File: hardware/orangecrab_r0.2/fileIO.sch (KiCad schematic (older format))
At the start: 26 parts, among them J1 Conn_01x12_Male, J2 Conn_01x16_Male, J3 USB_B_Micro, SW1 SW_Push, U9 CD74HC4067M

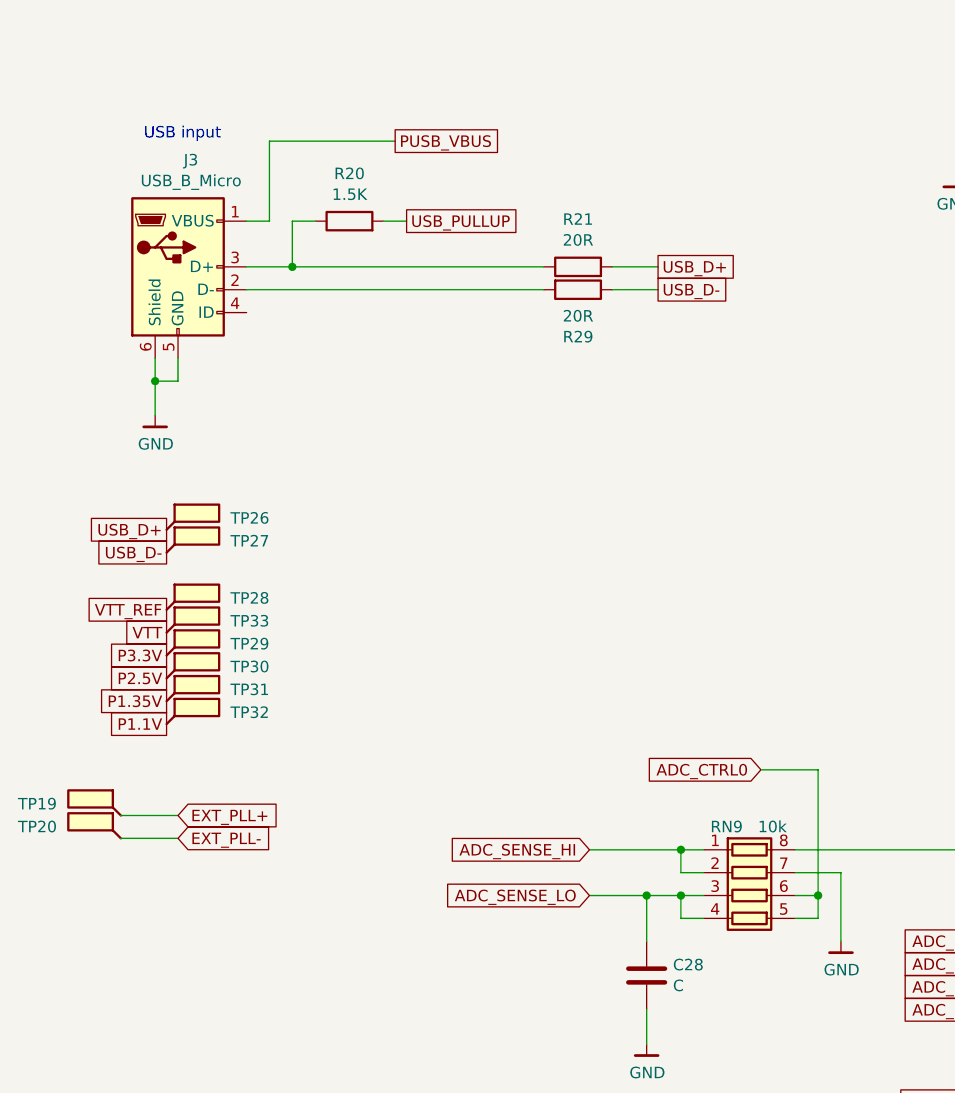
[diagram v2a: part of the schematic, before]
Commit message: hw: Update board with 3d models Finish pin-swaps and routing of open changes General cleanups
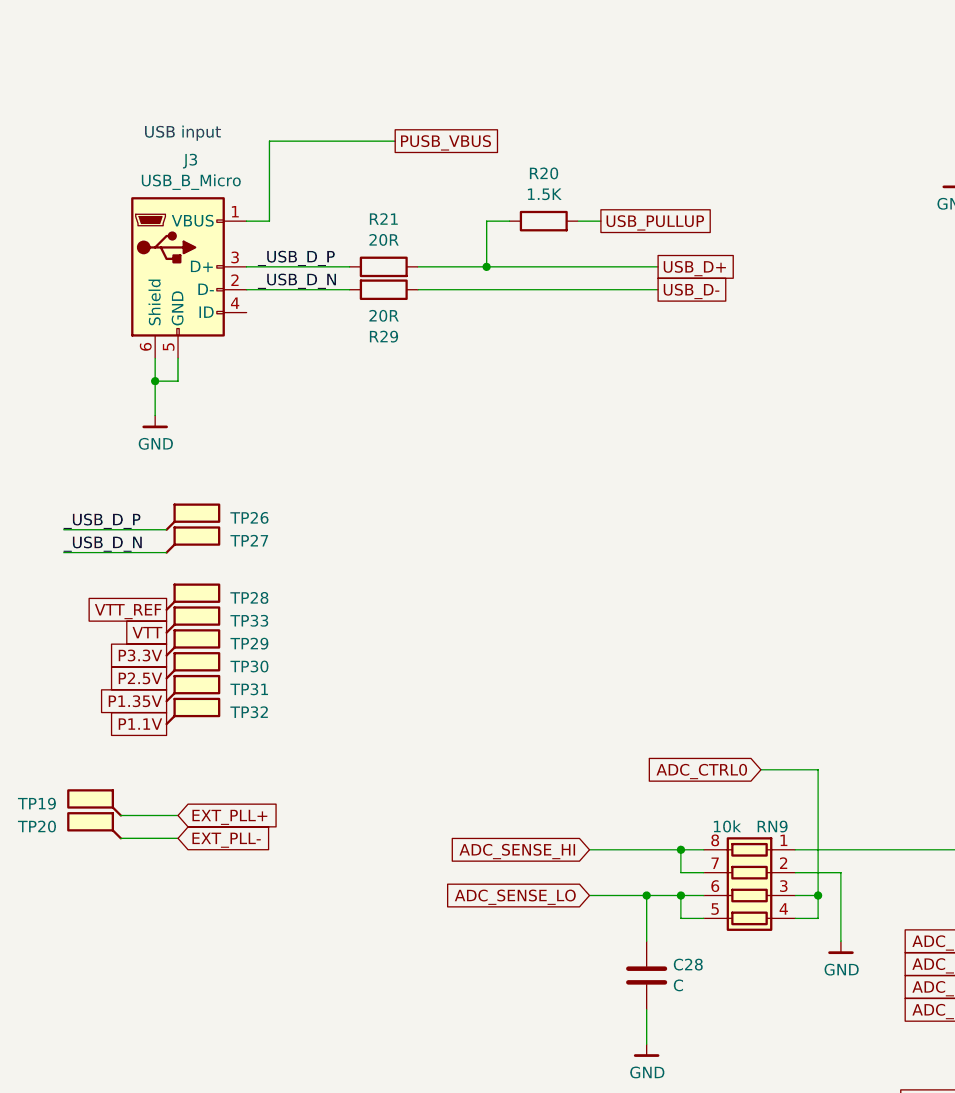
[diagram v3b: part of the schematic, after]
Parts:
- R21, R29: PN RC0201FR-071K5L -> (none)
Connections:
- net ADC_CTRL0: now also RN9.3 (R3.1), RN9.4 (R4.1); no longer RN9.5 (R4.2), RN9.6 (R3.2)
- net ADC_SENSE_HI: now also RN9.7 (R2.2), RN9.8 (R1.2); no longer RN9.1 (R1.1), RN9.2 (R2.1)
- net ADC_SENSE_LO: now also RN9.5 (R4.2), RN9.6 (R3.2); no longer RN9.3 (R3.1), RN9.4 (R4.1)
- net GND: now also RN9.2 (R2.1); no longer RN9.7 (R2.2)
- net USB_D+: now also R20.1; no longer TP26.1
- net USB_D-: no longer TP27.1
- net _USB_D_N: now reaches J3.2 (D-), R29.2
- net _USB_D_N: now also TP27.1
- net _USB_D_P: now reaches J3.3 (D+), R21.1
- net _USB_D_P: now also TP26.1; no longer R20.1
- net at U9.1 (COM): now also RN9.1 (R1.1); no longer RN9.8 (R1.2)
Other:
- moved on the sheet: R20, R21, R29
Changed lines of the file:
@@
 USB_D-
-Wire Wire Line
-	2100 1750 2300 1750
-Wire Wire Line
-	3900 1850 3700 1850
 Wire Wire Line
 	1800 2150 1800 2250
@@
 	1    0    0    -1
 $EndComp
-Text GLabel 2800 1550 2    50   UnSpc ~ 0
+Text GLabel 3650 1550 2    50   UnSpc ~ 0
 USB_PULLUP
 $Comp
 L Device:R R20
 U 1 1 5D4D2223
-P 2550 1550
-F 0 "R20" V 2757 1550 50  0000 C CNN
-F 1 "1.5K" V 2666 1550 50  0000 C CNN
-F 2 "Resistor_SMD:R_0201_0603Metric" V 2480 1550 50  0001 C CNN
-F 3 "~" H 2550 1550 50  0001 C CNN
-F 4 "‎Yageo‎" H 2550 1550 50  0001 C CNN "Mfg"
-F 5 "RC0201FR-071K5L" H 2550 1550 50  0001 C CNN "PN"
-	1    2550 1550
+P 3400 1550
+F 0 "R20" V 3607 1550 50  0000 C CNN
+F 1 "1.5K" V 3516 1550 50  0000 C CNN
+F 2 "Resistor_SMD:R_0201_0603Metric" V 3330 1550 50  0001 C CNN
+F 3 "~" H 3400 1550 50  0001 C CNN
+F 4 "‎Yageo‎" H 3400 1550 50  0001 C CNN "Mfg"
+F 5 "RC0201FR-071K5L" H 3400 1550 50  0001 C CNN "PN"
+	1    3400 1550
 	0    -1   -1   0
 $EndComp
 Wire Wire Line
-	2400 1550 2300 1550
-Wire Wire Line
-	2300 1550 2300 1750
-Connection ~ 2300 1750
-Wire Wire Line
-	2300 1750 3400 1750
-Wire Wire Line
-	2700 1550 2800 1550
+	3250 1550 3150 1550
+Wire Wire Line
+	3150 1550 3150 1750
+Wire Wire Line
+	3550 1550 3650 1550
 Wire Wire Line
 	2100 1550 2200 1550
@@
 	1    0    0    -1
 $EndComp
-Text GLabel 1750 2900 0    50   UnSpc ~ 0
-USB_D+
-Text GLabel 1750 3000 0    50   UnSpc ~ 0
-USB_D-
 $Comp
 L Connector:TestPoint_Flag TP31
@@
 L Device:R R21
 U 1 1 5DEC8B60
-P 3550 1750
-F 0 "R21" V 3757 1750 50  0000 C CNN
-F 1 "20R" V 3666 1750 50  0000 C CNN
-F 2 "Resistor_SMD:R_0201_0603Metric" V 3480 1750 50  0001 C CNN
-F 3 "~" H 3550 1750 50  0001 C CNN
-F 4 "‎Yageo‎" H 3550 1750 50  0001 C CNN "Mfg"
-F 5 "RC0201FR-071K5L" H 3550 1750 50  0001 C CNN "PN"
-	1    3550 1750
+P 2700 1750
+F 0 "R21" V 2907 1750 50  0000 C CNN
+F 1 "20R" V 2816 1750 50  0000 C CNN
+F 2 "Resistor_SMD:R_0201_0603Metric" V 2630 1750 50  0001 C CNN
+F 3 "~" H 2700 1750 50  0001 C CNN
+F 4 "‎Yageo‎" H 2700 1750 50  0001 C CNN "Mfg"
+	1    2700 1750
 	0    -1   -1   0
 $EndComp
-Wire Wire Line
-	3700 1750 3900 1750
 $Comp
 L Device:R R29
 U 1 1 5DECD575
-P 3550 1850
-F 0 "R29" V 3757 1850 50  0000 C CNN
-F 1 "20R" V 3666 1850 50  0000 C CNN
-F 2 "Resistor_SMD:R_0201_0603Metric" V 3480 1850 50  0001 C CNN
-F 3 "~" H 3550 1850 50  0001 C CNN
-F 4 "‎Yageo‎" H 3550 1850 50  0001 C CNN "Mfg"
-F 5 "RC0201FR-071K5L" H 3550 1850 50  0001 C CNN "PN"
-	1    3550 1850
+P 2700 1850
+F 0 "R29" V 2907 1850 50  0000 C CNN
+F 1 "20R" V 2816 1850 50  0000 C CNN
+F 2 "Resistor_SMD:R_0201_0603Metric" V 2630 1850 50  0001 C CNN
+F 3 "~" H 2700 1850 50  0001 C CNN
+F 4 "‎Yageo‎" H 2700 1850 50  0001 C CNN "Mfg"
+	1    2700 1850
 	0    1    1    0
 $EndComp
-Wire Wire Line
-	3400 1850 2100 1850
 $Comp
 L 74xx:CD74HC4067M U9
@@
 F 4 "Stackpole Electronics Inc" H 4300 4500 50  0001 C CNN "Mfg"
 	1    4300 4500
-	0    1    1    0
+	0    -1   1    0
 $EndComp
 Wire Wire Line
@@
 Wire Wire Line
 	6550 5300 6550 5200
+Connection ~ 3150 1750
+Wire Wire Line
+	2100 1750 2550 1750
+Wire Wire Line
+	2850 1750 3150 1750
+Wire Wire Line
+	2550 1850 2100 1850
+Wire Wire Line
+	2850 1850 3900 1850
+Wire Wire Line
+	3150 1750 3900 1750
+Text Label 2150 1750 0    50   ~ 0
+_USB_D_P
+Text Label 2150 1850 0    50   ~ 0
+_USB_D_N
+Text Label 1300 2900 0    50   ~ 0
+_USB_D_P
+Text Label 1300 3000 0    50   ~ 0
+_USB_D_N
+Wire Wire Line
+	1750 2900 1300 2900
+Wire Wire Line
+	1300 3000 1750 3000
 $EndSCHEMATC

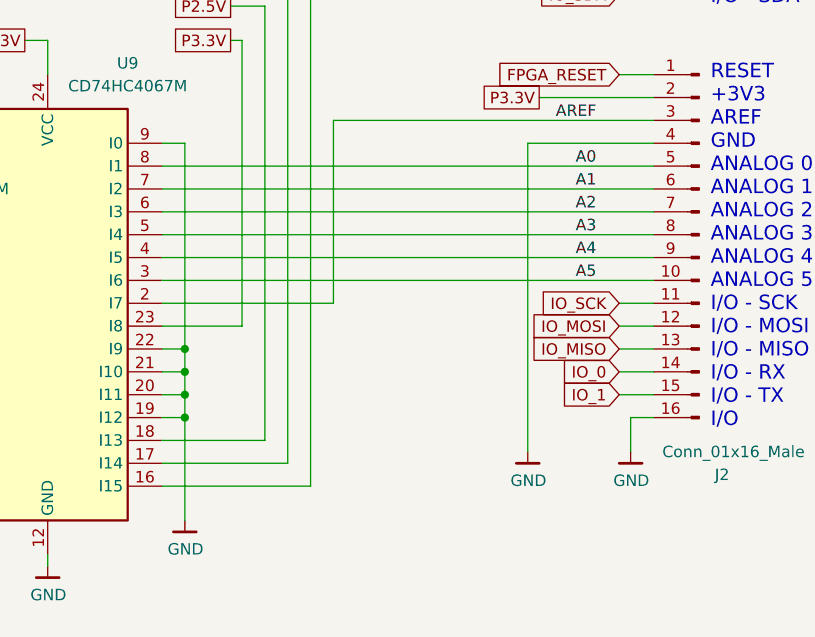
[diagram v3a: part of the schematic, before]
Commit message: hw: Route last FPGA I/O to A[0-5]
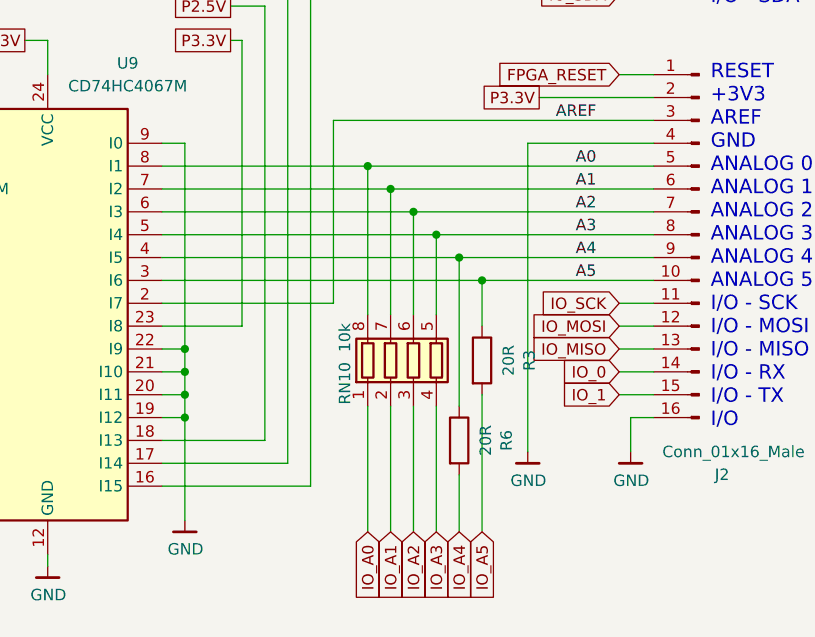
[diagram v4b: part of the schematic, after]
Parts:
- added R3, R6: 20R, Resistor_SMD:R_0201_0603Metric, symbol Device:R
- added RN10: 10k, Resistor_SMD:R_Array_Convex_4x0402, symbol Device:R_Pack04
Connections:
- net A0: now also RN10.8 (R1.2)
- net A1: now also RN10.7 (R2.2)
- net A2: now also RN10.6 (R3.2)
- net A3: now also RN10.5 (R4.2)
- net A4: now also R6.1
- net A5: now also R3.1
- new net IO_A0: RN10.1 (R1.1)
- new net IO_A1: RN10.2 (R2.1)
- new net IO_A2: RN10.3 (R3.1)
- new net IO_A3: RN10.4 (R4.1)
- new net IO_A4: R6.2
- new net IO_A5: R3.2
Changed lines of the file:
@@
 	6550 4100 6450 4100
 Wire Wire Line
-	6450 4200 8600 4200
-Wire Wire Line
-	6450 4300 8600 4300
-Wire Wire Line
-	6450 4400 8600 4400
-Wire Wire Line
-	6450 4500 8600 4500
-Wire Wire Line
-	6450 4600 8600 4600
-Wire Wire Line
-	6450 4700 8600 4700
+	6450 4200 7350 4200
+Wire Wire Line
+	6450 4300 7450 4300
+Wire Wire Line
+	6450 4400 7550 4400
+Wire Wire Line
+	6450 4500 7650 4500
+Wire Wire Line
+	6450 4700 7850 4700
 $Comp
 L gkl_power:GND #PWR0131
@@
 Wire Wire Line
 	1300 3000 1750 3000
+Text GLabel 7350 5800 3    50   Input ~ 0
+IO_A0
+Text GLabel 7450 5800 3    50   Input ~ 0
+IO_A1
+Text GLabel 7550 5800 3    50   Input ~ 0
+IO_A2
+Text GLabel 7650 5800 3    50   Input ~ 0
+IO_A3
+Text GLabel 7750 5800 3    50   Input ~ 0
+IO_A4
+Text GLabel 7850 5800 3    50   Input ~ 0
+IO_A5
+Wire Wire Line
+	7350 5800 7350 5250
+Connection ~ 7350 4200
+Wire Wire Line
+	7350 4200 8600 4200
+Wire Wire Line
+	7450 5800 7450 5250
+Connection ~ 7450 4300
+Wire Wire Line
+	7450 4300 8600 4300
+Wire Wire Line
+	7550 5800 7550 5250
+Connection ~ 7550 4400
+Wire Wire Line
+	7550 4400 8600 4400
+Wire Wire Line
+	7650 5800 7650 5250
+Connection ~ 7650 4500
+Wire Wire Line
+	7650 4500 8600 4500
+Wire Wire Line
+	7750 5800 7750 5550
+Wire Wire Line
+	7850 5800 7850 5200
+Connection ~ 7850 4700
+Wire Wire Line
+	7850 4700 8600 4700
+Wire Wire Line
+	7350 4850 7350 4200
+Wire Wire Line
+	7450 4850 7450 4300
+Wire Wire Line
+	7550 4850 7550 4400
+Wire Wire Line
+	7650 4850 7650 4500
+$Comp
+L Device:R R6
+U 1 1 5E8EF689
+P 7750 5400
+F 0 "R6" V 7957 5400 50  0000 C CNN
+F 1 "20R" V 7866 5400 50  0000 C CNN
+F 2 "Resistor_SMD:R_0201_0603Metric" V 7680 5400 50  0001 C CNN
+F 3 "~" H 7750 5400 50  0001 C CNN
+F 4 "‎Yageo‎" H 7750 5400 50  0001 C CNN "Mfg"
+	1    7750 5400
+	1    0    0    -1
+$EndComp
+$Comp
+L Device:R R3
+U 1 1 5E903005
+P 7850 5050
+F 0 "R3" V 8057 5050 50  0000 C CNN
+F 1 "20R" V 7966 5050 50  0000 C CNN
+F 2 "Resistor_SMD:R_0201_0603Metric" V 7780 5050 50  0001 C CNN
+F 3 "~" H 7850 5050 50  0001 C CNN
+F 4 "‎Yageo‎" H 7850 5050 50  0001 C CNN "Mfg"
+	1    7850 5050
+	1    0    0    -1
+$EndComp
+Wire Wire Line
+	7850 4900 7850 4700
+Wire Wire Line
+	6450 4600 7750 4600
+Wire Wire Line
+	7750 4600 8600 4600
+Connection ~ 7750 4600
+Wire Wire Line
+	7750 5250 7750 4600
+$Comp
+L Device:R_Pack04 RN?
+U 1 1 5E8ECDF4
+P 7550 5050
+AR Path="/5ABD38F2/5E8ECDF4" Ref="RN?"  Part="1"
+AR Path="/5ABC9A87/5E8ECDF4" Ref="RN10"  Part="1"
+F 0 "RN10" V 7250 4950 50  0000 C CNN
+F 1 "10k" V 7250 5150 50  0000 C CNN
+F 2 "Resistor_SMD:R_Array_Convex_4x0402" V 7825 5050 50  0001 C CNN
+F 3 "~" H 7550 5050 50  0001 C CNN
+F 4 "Stackpole Electronics Inc" H 7550 5050 50  0001 C CNN "Mfg"
+	1    7550 5050
+	1    0    0    -1
+$EndComp
 $EndSCHEMATC
